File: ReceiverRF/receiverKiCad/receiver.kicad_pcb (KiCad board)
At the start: 2 copper layers, 100 x 116.6 mm, 83 parts, among them J1 RF2-03E-T-00-50-G, J2 Conn_01x05_Socket, J3 Conn_01x02_Socket, J4 Conn_01x04, Q1 MMBT3904, Q2 PMOS, SW1 SW_Push, SW2 SW_Push, SW3 SW_Push, SW4 SW_Push, SW5 SW_SPDT, U1 STM32F103RET6, U2 NCV5501DT33RKG, U3 NJM2882F05-TE1, U4 MLX90393SLW-ABA-011-RE, U5 TXS0102DCUR, Y1 CTX853CT-ND

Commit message: Final layout and routing
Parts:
- added G***: LOGO, Footprints:logo, B.Cu at (165.5, 49.4)
- moved G*** 98.6 mm to (140.2, 149.9)
- moved SW3 38.7 mm to (136.4, 135.8)
- moved SW4 38.5 mm to (136.4, 110.9)
- moved BUT_R4 35.5 mm to (139.4, 107.9)
- moved BUT_R3 30.7 mm to (139.7, 132.2)
- moved SW2 29.8 mm to (167.9, 135.8)
- moved SW1 29.8 mm to (167.9, 110.9)
- moved BUT_R1 22.6 mm to (171.2, 107.9)
- moved BUT_R2 22.5 mm to (171.4, 132.8)
- moved REF** 1.71 mm to (155.2, 122.9)
- moved MLX_C1 0.54 mm to (177.3, 69.7)
- moved REF** 0.30 mm to (155.2, 125.5)
- moved STM_C5 0.26 mm to (172.0, 54.2)
- moved REF** 0.18 mm to (155.9, 64.0)
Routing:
- net +3.3V: track 36.2 -> 224.5 mm
- net +3.3V_IB: track 0.00 -> 136.3 mm, vias 0 -> 7
- net +5V_IB: track 0.00 -> 128.5 mm, vias 0 -> 2
- net VCC: track 9.83 -> 76.6 mm
- net BUZZER_IB: track 0.00 -> 61.6 mm, vias 0 -> 1
- net PUSH_2_IB: track 0.00 -> 56.7 mm, vias 0 -> 1
- net PUSH_3_IB: track 0.00 -> 56.3 mm, vias 0 -> 1
- net I2C_SDA_IB: track 0.00 -> 51.1 mm, vias 0 -> 2
- net I2C_SCL_IB: track 0.00 -> 45.6 mm, vias 0 -> 2
- net I2C_SDA: track 0.00 -> 39.8 mm, vias 0 -> 2
- net Net-(BUZ_D1-K): track 0.00 -> 39.5 mm
- net I2C_SCL: track 0.46 -> 37.1 mm, vias 0 -> 2
- net RFM_GPIO3: track 0.00 -> 35.2 mm, vias 0 -> 1
- net RFM_GPIO2: track 0.00 -> 31.7 mm, vias 0 -> 1
- net SPI_MOSI: track 0.00 -> 31.0 mm, vias 0 -> 2
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- added copper zone on F.Cu, net GND
- added copper zone on B.Cu, net GND_IB
- added copper zone on F.Cu, net GND_IB
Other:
- board size 100 x 116.6 mm -> 100 x 116.7 mm
- board text added: "I2C"
- board text added: "IDÉFIX V2 - Beacon/Receiver E2025 Victor Deschênes Christopher Smith"
- board text added: "IDÉFIX V2 - Interface Board E2025 Victor Deschênes Christopher Smith"
- board text added: "RX"
- board text added: "TX"
- board text removed: "IDÉFIX V1 H2025 Victor Deschênes"
- board text removed: "LCD"

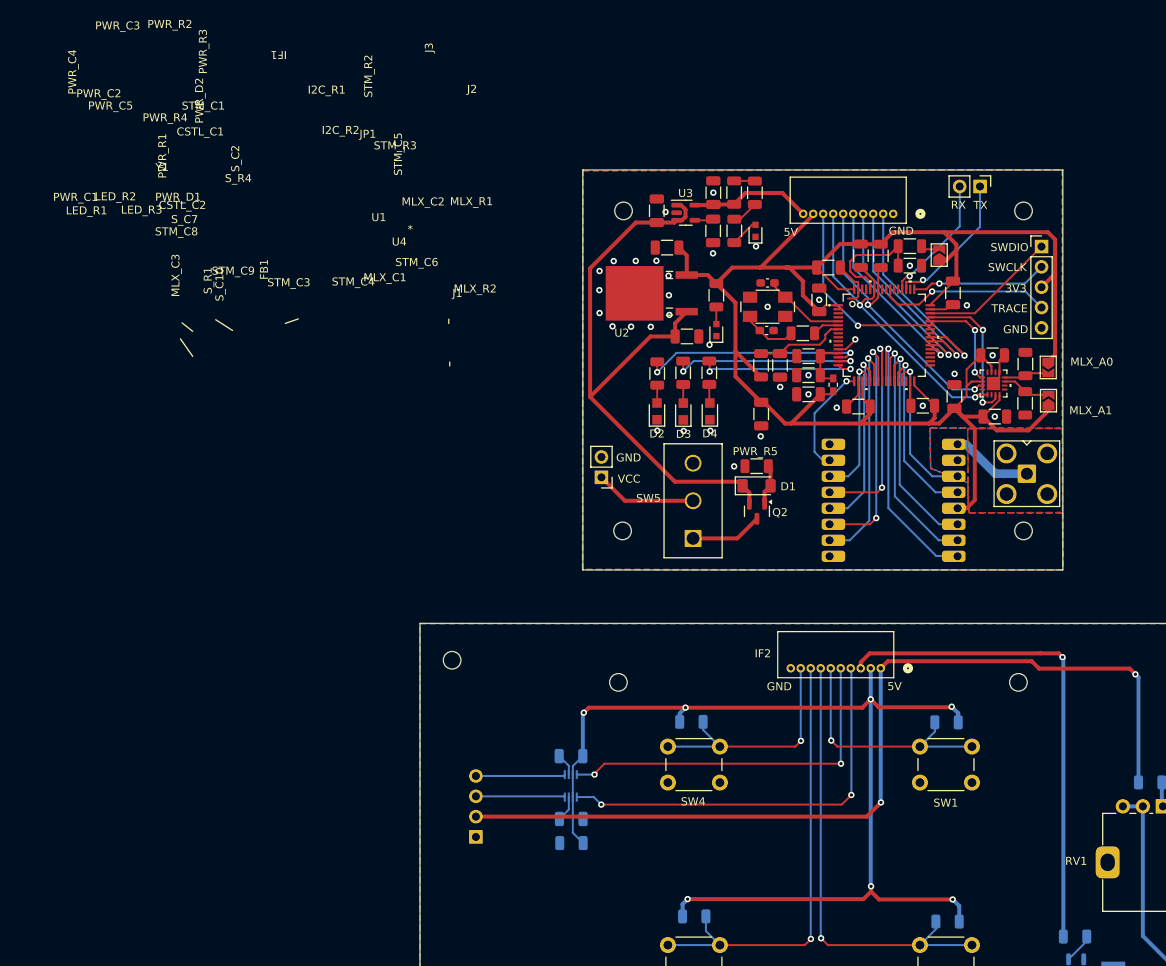
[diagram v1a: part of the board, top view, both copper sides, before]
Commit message: finished silkscreen and added logos
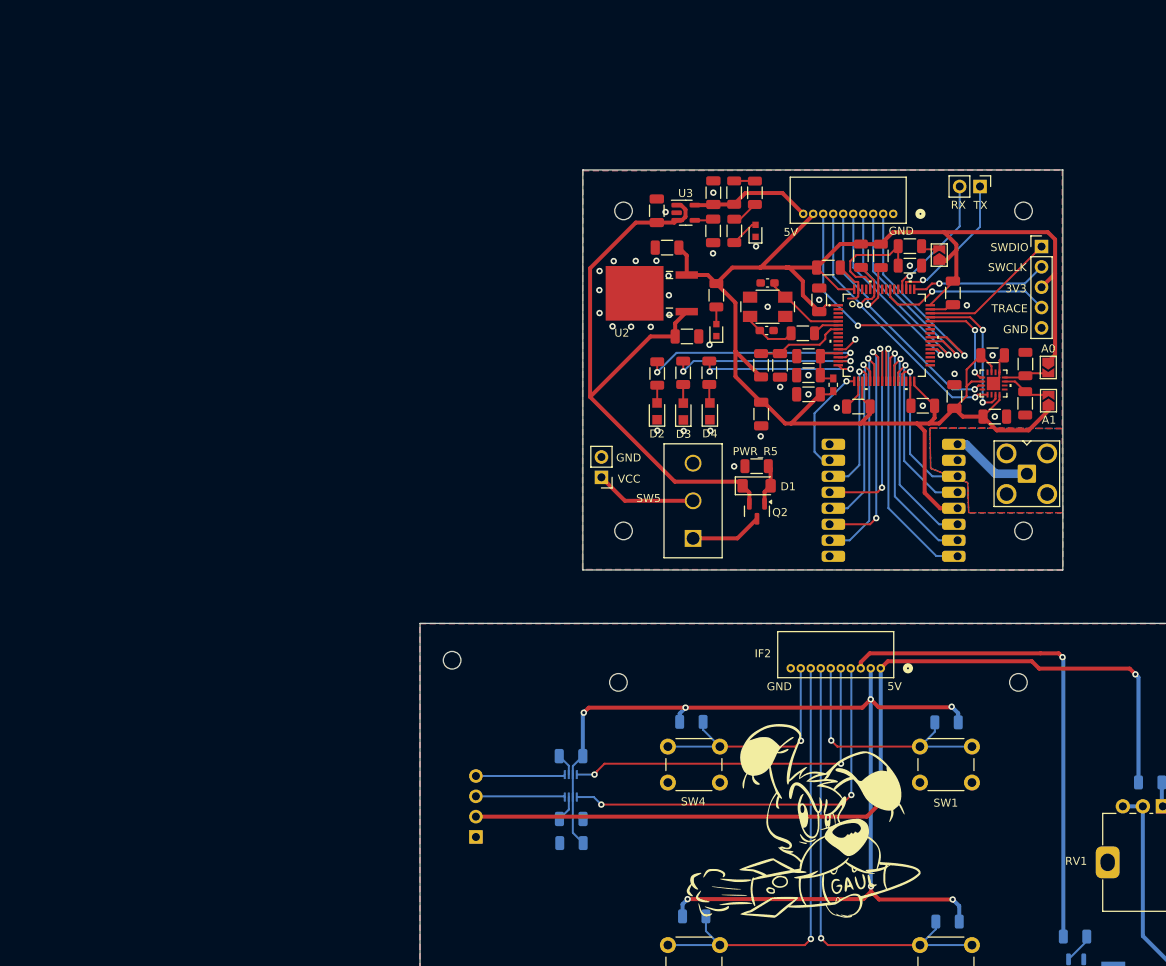
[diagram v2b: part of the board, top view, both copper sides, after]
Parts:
- added G***: LOGO, LOGO, F.Cu at (153.6, 119.8)
- added G***: LOGO, LOGO, B.Cu at (141.1, 56.2)
- D1: value BZV55C18 -> SZMMSZ4679T1G
- PWR_D1: value LED_0805_2012Metric -> LTST-C190EKT
- Q2: value PMOS -> NTR4101PT1G
- moved G*** 4.54 mm to (165.8, 53.9)
- renumbered REF** to HOLES1, REF** to HOLES2, REF** to HOLES3
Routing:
- net +3.3V: track 224.5 -> 223.3 mm
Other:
- board text added: "A0"
- board text added: "A1"
- board text added: "IdeFIX v2 Beacon / interface board"

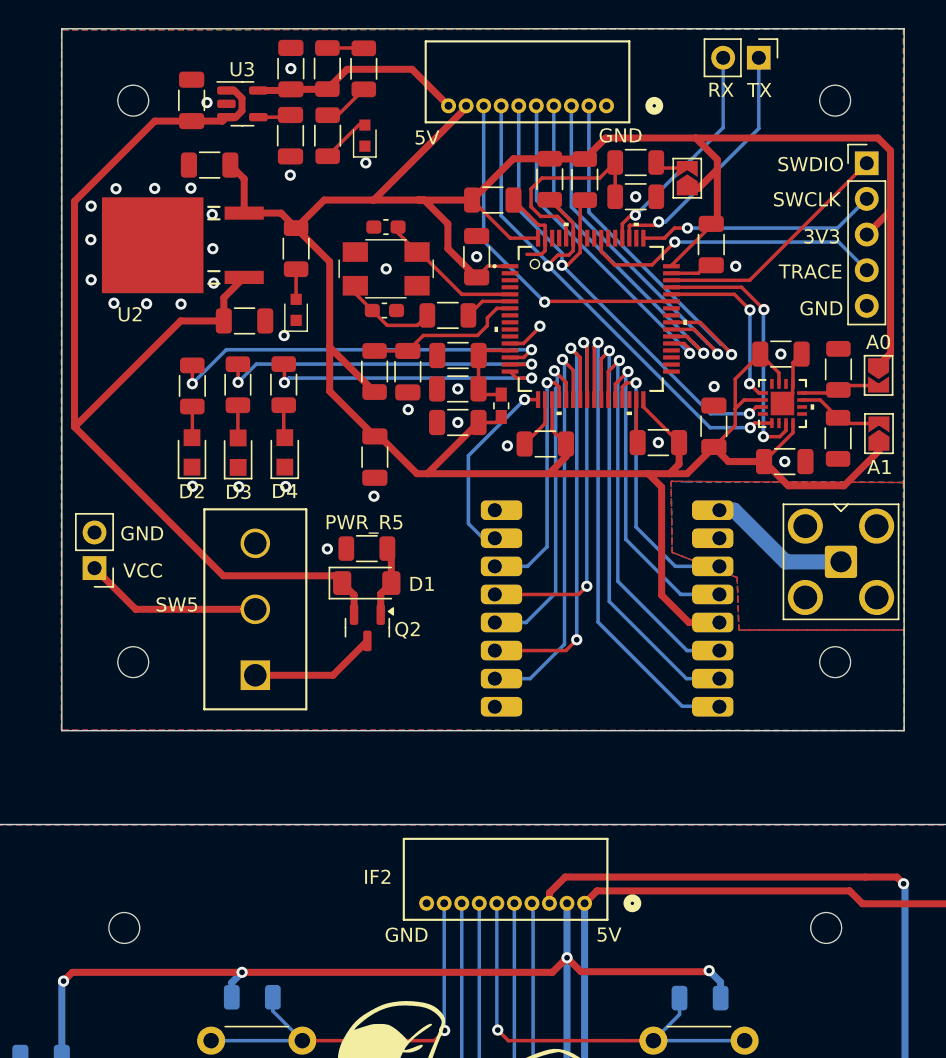
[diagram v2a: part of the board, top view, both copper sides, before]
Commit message: fix zener diode footprint, thermal relief on SMA conn, more work on silkscreen
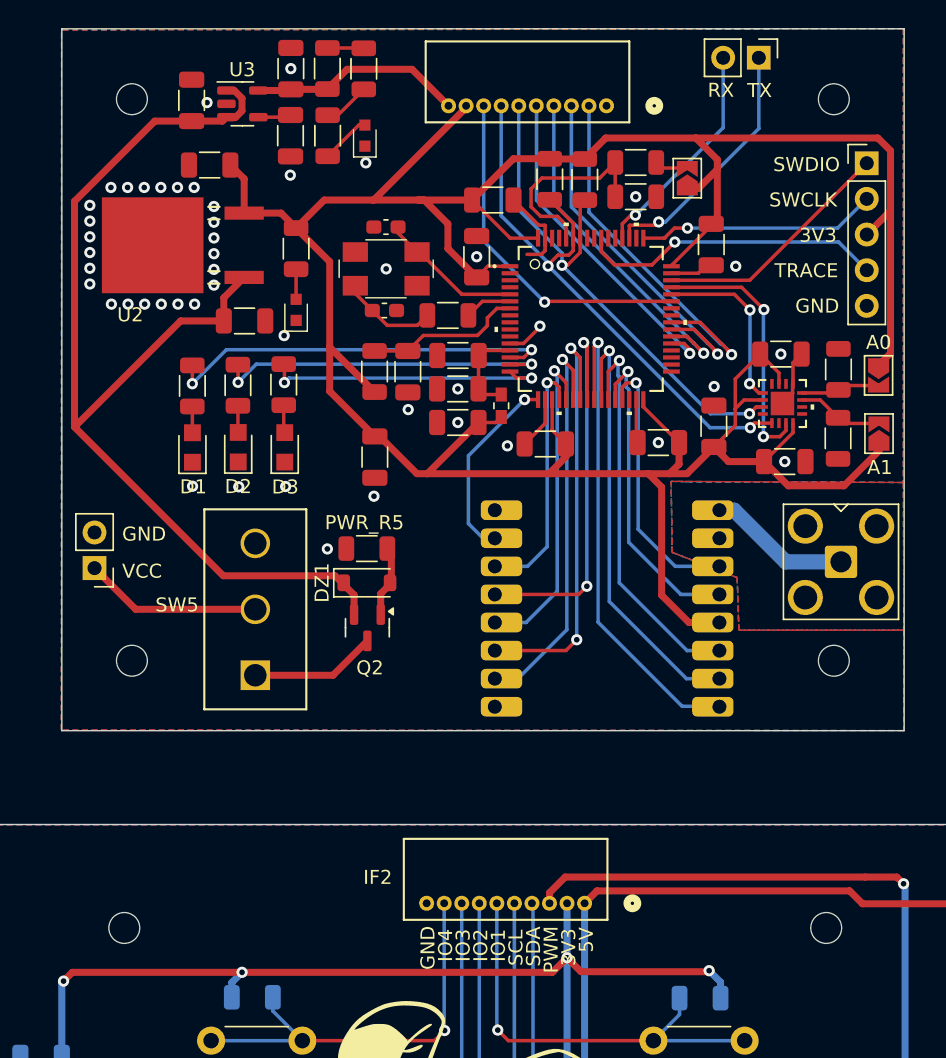
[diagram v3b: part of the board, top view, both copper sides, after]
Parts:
- removed D4: LTST-C170GKT, Footprints:LTST-C170GKT
- added DZ1: SZMMSZ4679T1G, Diode_SMD:D_SOD-123, F.Cu at (147.5, 78.3)
- D1: value SZMMSZ4679T1G -> LTST-C170GKT; footprint Diode_SMD:D_MiniMELF -> Footprints:LTST-C170GKT
- moved D1 15.7 mm to (135.1, 68.7), turned to 90 degrees
- moved D3 3.34 mm to (141.7, 68.7)
- moved D2 3.31 mm to (138.3, 68.7)
- moved HOLES1 0.14 mm to (155.8, 63.9)
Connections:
- D1 pad 1: VCC -> GND
- LED_R1 pad 2: Net-(D2-A) -> Net-(D1-A)
- LED_R2 pad 2: Net-(D3-A) -> Net-(D2-A)
- LED_R3 pad 2: Net-(D4-A) -> Net-(D3-A)
- PWR_R5 pad 1: Net-(D1-A) -> Net-(DZ1-A)
- Q2 pad 2: Net-(D1-A) -> Net-(DZ1-A)
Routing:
- net Net-(DZ1-A): track 0.00 -> 5.13 mm
- net Net-(D1-A): track 5.13 -> 1.91 mm
- net Net-(D4-A): track 2.34 -> 0.00 mm
- net GND: vias 35 -> 47
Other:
- board text added: "ANT"
- board text added: "CS"
- board text added: "IO1"
- board text added: "IO2"
- board text added: "IO3"
- board text added: "IO4"
- board text added: "MISO"
- board text added: "MOSI"
- board text added: "NIRQ"
- board text added: "PWM"
- board text added: "SCK"
- board text added: "SDN"

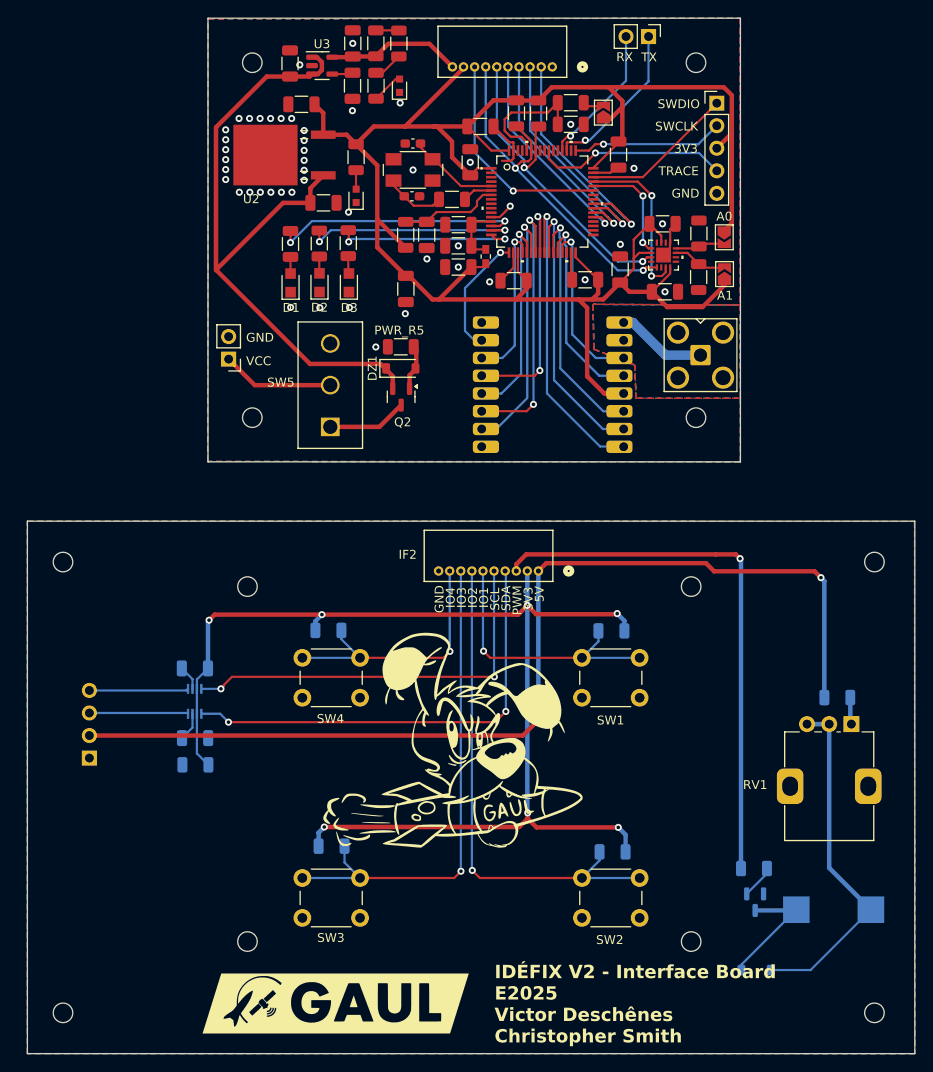
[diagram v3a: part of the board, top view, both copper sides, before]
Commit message: 3.2mm holes, XT30 connector, add polyfuse, minor fixes
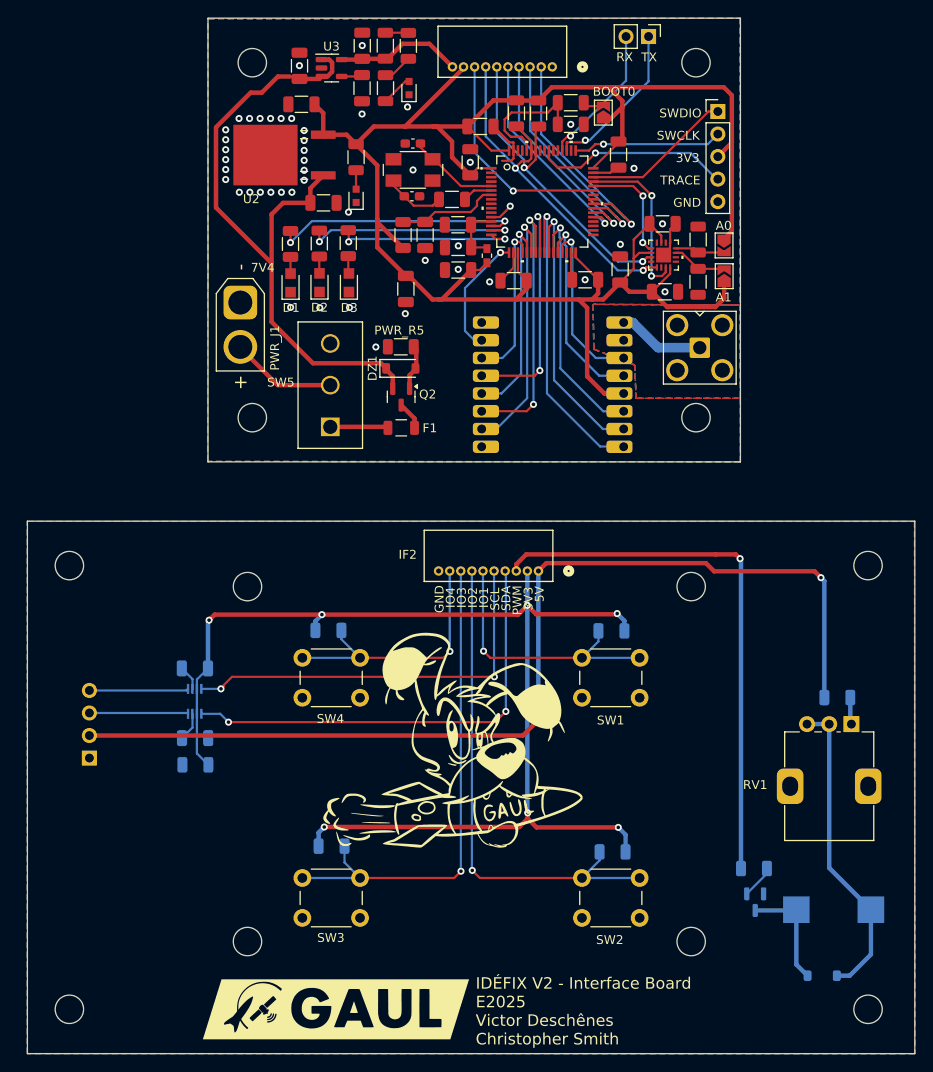
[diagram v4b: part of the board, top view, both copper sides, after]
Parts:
- added F1: Polyfuse, Footprints:Polyfuse, F.Cu at (147.6, 85.0)
- PWR_J1: value Conn_01x02 -> XT30; footprint Connector_PinHeader_2.54mm:PinHeader_1x02_P2.54mm_Vertical -> Connector_AMASS:AMASS_XT30U-M_1x02_P5.0mm_Vertical
- Y1: value CTX853CT-ND -> 406C35D08M00000
- moved BUZ_D1 7.48 mm to (195.0, 146.8)
- moved PWR_J1 6.51 mm to (129.4, 70.9), turned to -90 degrees
- moved PWR_C3 1.10 mm to (143.2, 42.0)
- moved PWR_C4 1.10 mm to (136.1, 44.2)
- moved PWR_R3 1.10 mm to (148.4, 42.0)
- moved U3 1.10 mm to (139.7, 44.5)
- moved PWR_C5 1.10 mm to (143.1, 46.7)
- moved PWR_D2 1.10 mm to (148.4, 46.7)
- moved PWR_R2 1.10 mm to (145.8, 42.0)
- moved PWR_R4 1.10 mm to (145.8, 46.7)
- moved J2 0.94 mm to (183.2, 49.4)
- moved MLX_A0 0.92 mm to (183.9, 64.5)
- moved J1 0.85 mm to (181.2, 76.0)
- moved MLX_R1 0.69 mm to (181.0, 63.8)
- moved G*** 0.65 mm to (140.2, 150.5)
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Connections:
- PWR_J1 pad 1: Net-(PWR_J1-Pin_1) -> GND
- PWR_J1 pad 2: GND -> Net-(PWR_J1-Pin_2)
- SW5 pad 1: Net-(Q2-D) -> Net-(SW5-A)
- SW5 pad 2: Net-(PWR_J1-Pin_1) -> Net-(PWR_J1-Pin_2)
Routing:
- net Net-(PWR_J1-Pin_1): track 12.7 -> 0.00 mm
- net Net-(PWR_J1-Pin_2): track 0.00 -> 12.0 mm
- net Net-(SW5-A): track 0.00 -> 6.54 mm
- net Net-(Q2-D): track 9.00 -> 3.18 mm
- net Net-(BUZ_D1-K): track 39.5 -> 35.2 mm
- net VCC: track 76.6 -> 73.4 mm
- net +3.3V: track 223.3 -> 225.8 mm
- net Net-(BUZ_D1-A): track 14.1 -> 12.6 mm
- net +5V: track 15.3 -> 14.3 mm
- net Net-(MLX_A1-B): track 6.17 -> 6.97 mm
- net +3.3VA: track 6.55 -> 7.35 mm
- net Net-(MLX_A0-B): track 5.67 -> 6.39 mm
- net SYS_TRACESWO: track 21.8 -> 22.3 mm
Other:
- board text added: "7V4"
- board text added: "BOOT0"
- board text removed: "VCC"
